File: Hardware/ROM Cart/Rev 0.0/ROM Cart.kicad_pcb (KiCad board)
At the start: 2 copper layers, 81.8 x 57.6 mm, 12 parts, among them J1 6502 Card Edge, U1 AT27C256, U2 74HC138

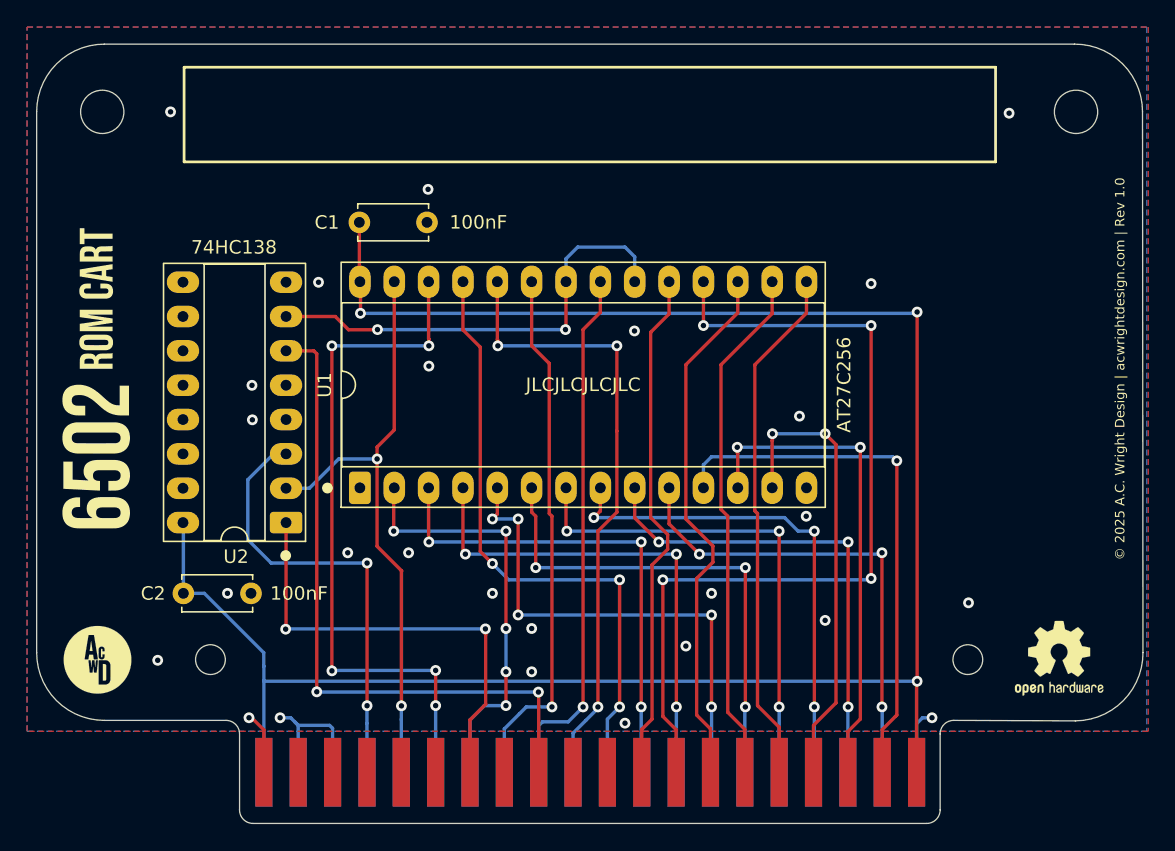
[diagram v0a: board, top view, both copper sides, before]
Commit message: Use 27C256 for ROMCart
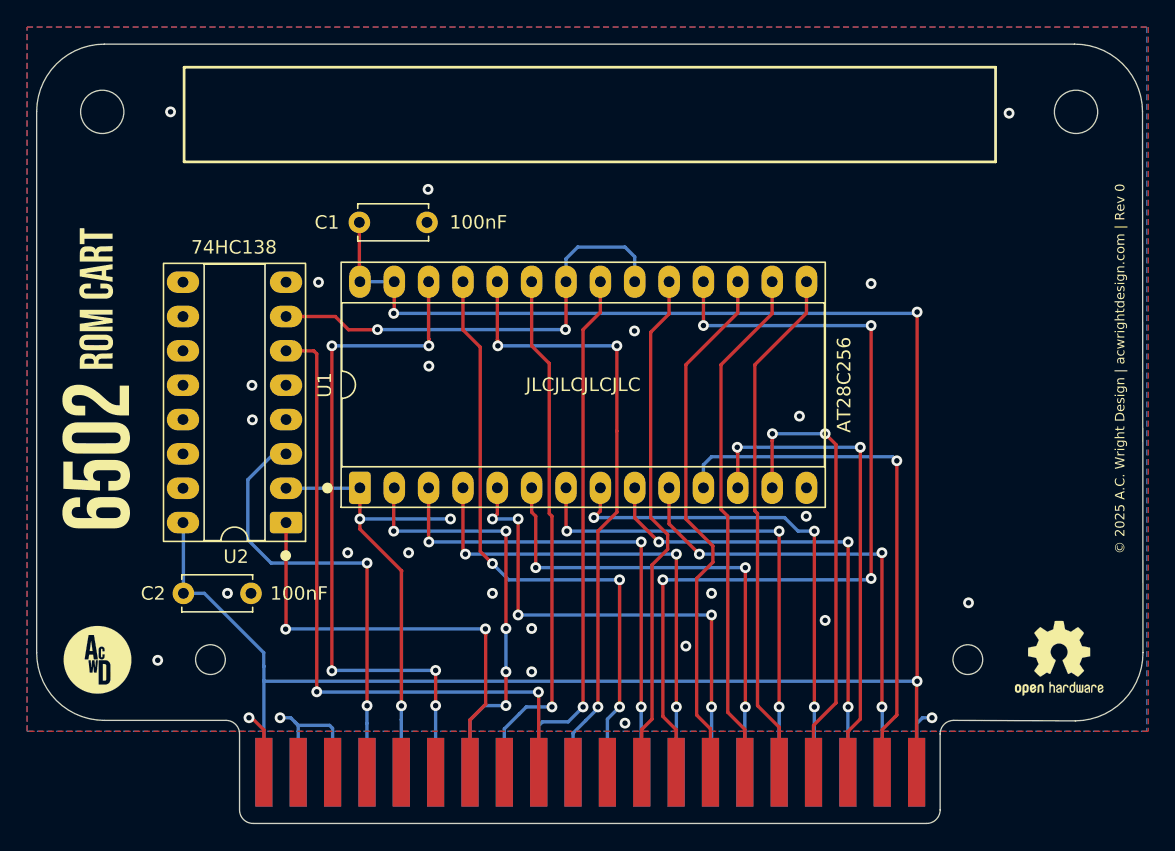
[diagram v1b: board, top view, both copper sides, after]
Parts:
- U1: value AT27C256 -> AT28C256
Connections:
- net REB renamed RB
- U1 pad 1: unconnected-(U1-VPP-Pad1) -> A14
- U1 pad 27: A14 -> VCC
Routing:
- net A14: track 45.2 -> 34.6 mm, vias 2 -> 3
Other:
- board text added: "© 2025 A.C. Wright Design | acwrightdesign.com | Rev 0"
- board text removed: "© 2025 A.C. Wright Design | acwrightdesign.com | Rev 1.0"
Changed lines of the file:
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@@
 	(title_block
 		(title "6502 ROM Cart")
-		(date "2026-03-22")
-		(rev "1.0")
+		(date "2025-09-17")
+		(rev "0.0")
 		(company "A.C. Wright Design")
 	)
@@
 	)
 	(net 0 "")
-	(net 1 "unconnected-(U1-VPP-Pad1)")
+	(net 1 "RB")
 	(net 2 "A3")
 	(net 3 "A0")
@@
 	(net 43 "unconnected-(J1-PadIRQB)")
 	(net 44 "unconnected-(J1-PadEXP3)")
-	(net 45 "REB")
 	(footprint "6502 Logos:6502 ROM Cart Logo 5mm"
 		(layer "F.Cu")
@@
 			(layers "*.Cu" "*.Mask")
 			(remove_unused_layers no)
-			(net 45 "REB")
+			(net 1 "RB")
 			(pinfunction "~{Y7}")
 			(pintype "output")
@@
 			)
 		)
-		(property "Value" "AT27C256"
+		(property "Value" "AT28C256"
 			(at 7.62 35.8 90)
 			(layer "F.SilkS")
@@
 		(sheetname "/")
 		(sheetfile "ROM Cart.kicad_sch")
-		(attr through_hole)
+		(attr through_hole exclude_from_bom)
 		(fp_line
 			(start 13.68 -1.33)
@@
 			(remove_unused_layers no)
 			(roundrect_rratio 0.15625)
-			(net 1 "unconnected-(U1-VPP-Pad1)")
-			(pinfunction "VPP")
-			(pintype "power_in+no_connect")
+			(net 25 "A14")
+			(pinfunction "A14")
+			(pintype "bidirectional")
 		)
 		(pad "2" thru_hole oval
@@
 			(layers "*.Cu" "*.Mask")
 			(remove_unused_layers no)
-			(net 45 "REB")
+			(net 1 "RB")
 			(pinfunction "~{CE}")
 			(pintype "bidirectional")
@@
 			(layers "*.Cu" "*.Mask")
 			(remove_unused_layers no)
-			(net 45 "REB")
+			(net 1 "RB")
 			(pinfunction "~{OE}")
 			(pintype "bidirectional")
@@
 			(layers "*.Cu" "*.Mask")
 			(remove_unused_layers no)
-			(net 25 "A14")
-			(pinfunction "A14")
+			(net 19 "VCC")
+			(pinfunction "~{WE}")
 			(pintype "bidirectional")
 		)
@@
 		(layer "Edge.Cuts")
 	)
-	(gr_text "© 2025 A.C. Wright Design | acwrightdesign.com | Rev 1.0"
+	(gr_text "© 2025 A.C. Wright Design | acwrightdesign.com | Rev 0"
 		(at 178.6 100.2 90)
 		(layer "F.SilkS")
@@
 	)
 	(segment
-		(start 122.37 109.03)
-		(end 122.4 109)
+		(start 123.69 97.31)
+		(end 123.7 97.3)
+		(width 0.25)
+		(layer "F.Cu")
+		(net 1)
+	)
+	(segment
+		(start 116.94 96.33)
+		(end 120.58 96.33)
+		(width 0.25)
+		(layer "F.Cu")
+		(net 1)
+	)
+	(segment
+		(start 121.56 97.31)
+		(end 123.69 97.31)
+		(width 0.25)
+		(layer "F.Cu")
+		(net 1)
+	)
+	(segment
+		(start 137.64 97.26)
+		(end 137.64 93.76)
+		(width 0.25)
+		(layer "F.Cu")
+		(net 1)
+	)
+	(segment
+		(start 120.58 96.33)
+		(end 121.56 97.31)
+		(width 0.25)
+		(layer "F.Cu")
+		(net 1)
+	)
+	(segment
+		(start 137.6 97.3)
+		(end 137.64 97.26)
+		(width 0.25)
+		(layer "F.Cu")
+		(net 1)
+	)
+	(via
+		(at 137.6 97.3)
+		(size 0.8)
+		(drill 0.4)
+		(layers "F.Cu" "B.Cu")
+		(net 1)
+	)
+	(via
+		(at 123.7 97.3)
+		(size 0.8)
+		(drill 0.4)
+		(layers "F.Cu" "B.Cu")
+		(net 1)
+	)
+	(segment
+		(start 142 91.2)
+		(end 142.72 91.92)
+		(width 0.25)
+		(layer "B.Cu")
+		(net 1)
+	)
+	(segment
+		(start 137.64 93.76)
+		(end 137.64 92.06)
+		(width 0.25)
+		(layer "B.Cu")
+		(net 1)
+	)
+	(segment
+		(start 137.64 92.06)
+		(end 138.5 91.2)
+		(width 0.25)
+		(layer "B.Cu")
+		(net 1)
+	)
+	(segment
+		(start 123.7 97.3)
+		(end 137.6 97.3)
+		(width 0.25)
+		(layer "B.Cu")
+		(net 1)
+	)
+	(segment
+		(start 142.72 91.92)
+		(end 142.72 93.76)
+		(width 0.25)
+		(layer "B.Cu")
+		(net 1)
+	)
+	(segment
+		(start 138.5 91.2)
+		(end 142 91.2)
 		(width 0.25)
 		(layer "B.Cu")
@@
 	)
 	(segment
-		(start 122.4411 96.0936)
-		(end 122.4411 93.8011)
+		(start 163.56 123.34)
+		(end 163.56 130.03)
 		(width 0.25)
 		(layer "F.Cu")
@@
 	)
 	(segment
-		(start 163.56 123.34)
-		(end 163.56 130.03)
+		(start 124.94 93.76)
+		(end 124.94 96.06)
 		(width 0.25)
 		(layer "F.Cu")
@@
 	)
 	(segment
-		(start 122.4411 93.8011)
-		(end 122.4 93.76)
+		(start 124.94 96.06)
+		(end 124.9 96.1)
 		(width 0.25)
 		(layer "F.Cu")
@@
 	)
 	(via
-		(at 163.6 96)
+		(at 124.9 96.1)
 		(size 0.8)
 		(drill 0.4)
@@
 	)
 	(via
-		(at 122.4411 96.0936)
+		(at 163.6 96)
 		(size 0.8)
 		(drill 0.4)
@@
 	)
 	(segment
-		(start 124.9 96.1)
-		(end 122.4475 96.1)
-		(width 0.25)
-		(layer "B.Cu")
-		(net 19)
-	)
-	(segment
 		(start 163.5 96.1)
 		(end 163.6 96)
@@
 	)
 	(segment
-		(start 122.4475 96.1)
-		(end 122.4411 96.0936)
-		(width 0.25)
-		(layer "B.Cu")
-		(net 19)
-	)
-	(segment
 		(start 115.3 130.03)
 		(end 115.3 123.27)
@@
 	)
 	(segment
+		(start 122.4 93.76)
+		(end 124.94 93.76)
+		(width 0.25)
+		(layer "B.Cu")
+		(net 19)
+	)
+	(segment
 		(start 115.29 121.19)
 		(end 110.9 116.8)
@@
 	)
 	(segment
-		(start 123.6711 105.9836)
-		(end 123.6711 106.8636)
+		(start 122.4 112.05)
+		(end 122.4 111.3)
 		(width 0.25)
 		(layer "F.Cu")
@@
 	)
 	(segment
-		(start 125.47 115.16)
-		(end 125.49 115.14)
+		(start 129.1 111.3)
+		(end 129.15 111.35)
 		(width 0.25)
 		(layer "F.Cu")
@@
 	)
 	(segment
-		(start 123.6711 113.3211)
+		(start 125.47 115.16)
 		(end 125.49 115.14)
 		(width 0.25)
@@
 	)
 	(segment
-		(start 124.94 93.76)
-		(end 124.94 104.7147)
+		(start 122.4 109)
+		(end 122.4 111.3)
 		(width 0.25)
 		(layer "F.Cu")
@@
 	)
 	(segment
-		(start 124.94 104.7147)
-		(end 123.6711 105.9836)
-		(width 0.25)
-		(layer "F.Cu")
-		(net 25)
-	)
-	(segment
-		(start 123.6711 106.8636)
-		(end 123.6711 113.3211)
+		(start 125.49 115.14)
+		(end 122.4 112.05)
 		(width 0.25)
 		(layer "F.Cu")
@@
 	)
 	(via
+		(at 129.1 111.3)
+		(size 0.8)
+		(drill 0.4)
+		(layers "F.Cu" "B.Cu")
+		(net 25)
+	)
+	(via
 		(at 125.47 125.12)
 		(size 0.8)
@@
 	)
 	(via
-		(at 123.6711 106.8636)
+		(at 122.4 111.3)
 		(size 0.8)
 		(drill 0.4)
@@
 	)
 	(segment
-		(start 118.6647 109.03)
-		(end 120.8311 106.8636)
+		(start 122.4 111.3)
+		(end 129.1 111.3)
 		(width 0.25)
 		(layer "B.Cu")
@@
 	)
 	(segment
-		(start 120.8311 106.8636)
-		(end 123.6711 106.8636)
+		(start 116.94 109.03)
+		(end 122.37 109.03)
 		(width 0.25)
 		(layer "B.Cu")
@@
 	)
 	(segment
-		(start 116.94 109.03)
-		(end 118.6647 109.03)
+		(start 122.37 109.03)
+		(end 122.4 109)
 		(width 0.25)
 		(layer "B.Cu")
@@
 		(net 36)
 	)
-	(segment
-		(start 123.69 97.31)
-		(end 123.7 97.3)
-		(width 0.25)
-		(layer "F.Cu")
-		(net 45)
-	)
-	(segment
-		(start 116.94 96.33)
-		(end 120.58 96.33)
-		(width 0.25)
-		(layer "F.Cu")
-		(net 45)
-	)
-	(segment
-		(start 121.56 97.31)
-		(end 123.69 97.31)
-		(width 0.25)
-		(layer "F.Cu")
-		(net 45)
-	)
-	(segment
-		(start 137.64 97.26)
-		(end 137.64 93.76)
-		(width 0.25)
-		(layer "F.Cu")
-		(net 45)
-	)
-	(segment
-		(start 120.58 96.33)
-		(end 121.56 97.31)
-		(width 0.25)
-		(layer "F.Cu")
-		(net 45)
-	)
-	(segment
-		(start 137.6 97.3)
-		(end 137.64 97.26)
-		(width 0.25)
-		(layer "F.Cu")
-		(net 45)
-	)
-	(via
-		(at 137.6 97.3)
-		(size 0.8)
-		(drill 0.4)
-		(layers "F.Cu" "B.Cu")
-		(net 45)
-	)
-	(via
-		(at 123.7 97.3)
-		(size 0.8)
-		(drill 0.4)
-		(layers "F.Cu" "B.Cu")
-		(net 45)
-	)
-	(segment
-		(start 142 91.2)
-		(end 142.72 91.92)
-		(width 0.25)
-		(layer "B.Cu")
-		(net 45)
-	)
-	(segment
-		(start 137.64 93.76)
-		(end 137.64 92.06)
-		(width 0.25)
-		(layer "B.Cu")
-		(net 45)
-	)
-	(segment
-		(start 137.64 92.06)
-		(end 138.5 91.2)
-		(width 0.25)
-		(layer "B.Cu")
-		(net 45)
-	)
-	(segment
-		(start 123.7 97.3)
-		(end 137.6 97.3)
-		(width 0.25)
-		(layer "B.Cu")
-		(net 45)
-	)
-	(segment
-		(start 142.72 91.92)
-		(end 142.72 93.76)
-		(width 0.25)
-		(layer "B.Cu")
-		(net 45)
-	)
-	(segment
-		(start 138.5 91.2)
-		(end 142 91.2)
-		(width 0.25)
-		(layer "B.Cu")
-		(net 45)
-	)
 	(zone
